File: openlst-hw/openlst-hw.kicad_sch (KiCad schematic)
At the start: 4 parts

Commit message: detailed power switches moved from EPS to invidual boards, each board only has core and aux bus (and batt if needed) which scales better. Reassign PC104 slots
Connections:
- no-connect marks 24 -> 20
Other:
- sheet CAN Bridge ports: added 3V3, 3V3_AUX, 3V3_COMM; removed VIO_CAN, VIO_CORE
- sheet INTERBOARD_CONNECTOR2 ports: added none; removed 3V3_17, 3V3_18, 3V3_19, 3V3_20

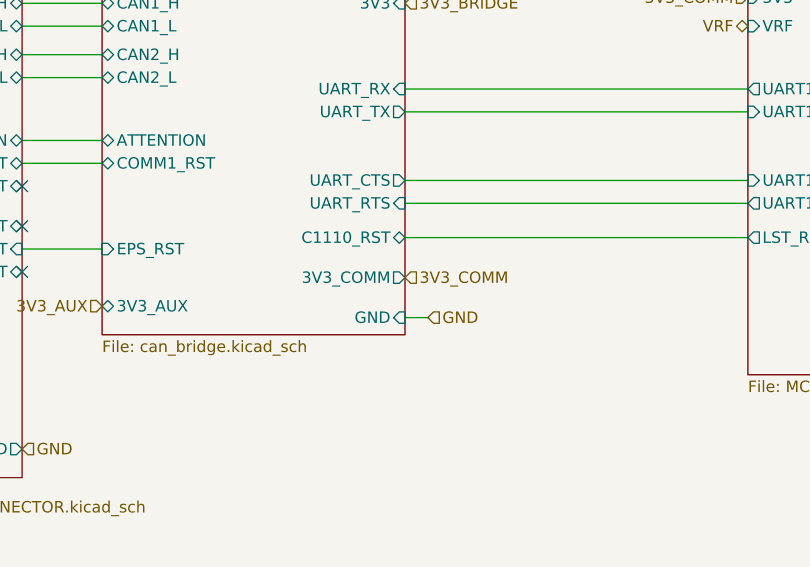
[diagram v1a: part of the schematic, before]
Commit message: rework COM board, add SPI ethernet for sat modem, upgrade all projects to 9.0.2
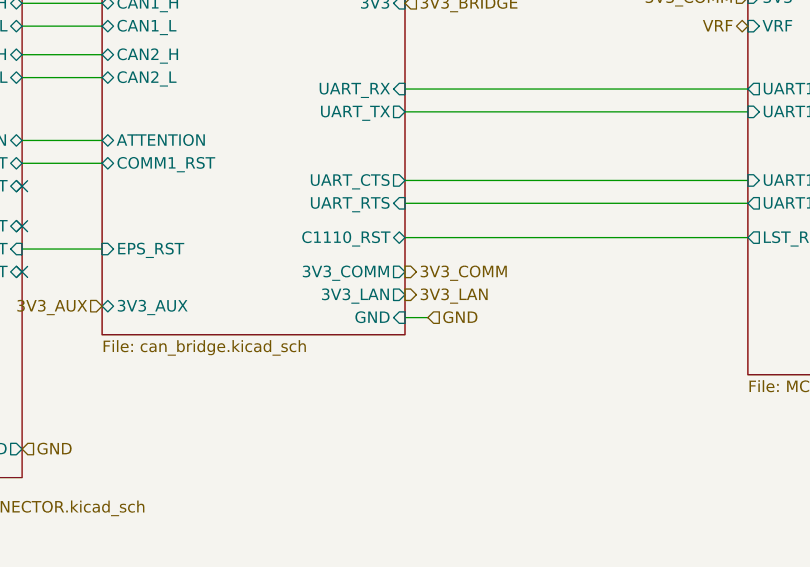
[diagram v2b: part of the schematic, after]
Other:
- sheet CAN Bridge ports: added 3V3_LAN; removed none
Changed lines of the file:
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@@
 (kicad_sch
-	(version 20231120)
+	(version 20250114)
 	(generator "eeschema")
-	(generator_version "8.0")
+	(generator_version "9.0")
 	(paper "A4")
 	(title_block
@@
 		(shape bidirectional)
 		(at 206.375 40.64 180)
-		(fields_autoplaced yes)
 		(effects
 			(font
@@
 		(shape output)
 		(at 109.855 108.585 180)
-		(fields_autoplaced yes)
 		(effects
 			(font
@@
 		(shape output)
 		(at 241.3 71.12 0)
-		(fields_autoplaced yes)
 		(effects
 			(font
@@
 		(shape bidirectional)
 		(at 154.305 40.005 180)
-		(fields_autoplaced yes)
 		(effects
 			(font
@@
 		)
 	)
+	(hierarchical_label "3V3_LAN"
+		(shape output)
+		(at 116.205 69.85 0)
+		(effects
+			(font
+				(size 1.27 1.27)
+			)
+			(justify left)
+		)
+	)
 	(hierarchical_label "GND"
 		(shape output)
 		(at 140.97 171.45 180)
-		(fields_autoplaced yes)
 		(effects
 			(font
@@
 		(shape input)
 		(at 45.72 52.705 180)
-		(fields_autoplaced yes)
 		(effects
 			(font
@@
 		(shape bidirectional)
 		(at 206.375 37.465 180)
-		(fields_autoplaced yes)
 		(effects
 			(font
@@
 		(shape output)
 		(at 191.135 76.835 0)
-		(fields_autoplaced yes)
 		(effects
 			(font
@@
 		(shape input)
 		(at 69.85 108.585 180)
-		(fields_autoplaced yes)
 		(effects
 			(font
@@
 		(shape input)
 		(at 118.745 72.39 0)
-		(fields_autoplaced yes)
 		(effects
 			(font
@@
 		(shape input)
 		(at 154.305 36.83 180)
-		(fields_autoplaced yes)
 		(effects
 			(font
@@
 		(shape input)
 		(at 98.425 108.585 180)
-		(fields_autoplaced yes)
 		(effects
 			(font
@@
 		(shape input)
 		(at 45.72 55.245 180)
-		(fields_autoplaced yes)
 		(effects
 			(font
@@
 		(shape input)
 		(at 116.205 37.465 0)
-		(fields_autoplaced yes)
 		(effects
 			(font
@@
 		(shape input)
 		(at 73.66 86.995 0)
-		(fields_autoplaced yes)
 		(effects
 			(font
@@
 		(shape input)
 		(at 86.36 108.585 180)
-		(fields_autoplaced yes)
 		(effects
 			(font
@@
 		(shape input)
 		(at 82.55 71.12 180)
-		(fields_autoplaced yes)
 		(effects
 			(font
@@
 		(shape input)
 		(at 45.72 29.21 180)
-		(fields_autoplaced yes)
 		(effects
 			(font
@@
 	)
 	(hierarchical_label "3V3_COMM"
-		(shape input)
-		(at 116.205 67.945 0)
-		(fields_autoplaced yes)
+		(shape output)
+		(at 116.205 67.31 0)
 		(effects
 			(font
@@
 		(at 45.72 24.13)
 		(size 27.94 66.04)
+		(exclude_from_sim no)
+		(in_bom yes)
+		(on_board yes)
+		(dnp no)
 		(stroke
 			(width 0)
@@
 		(at 82.55 34.925)
 		(size 33.655 39.37)
+		(exclude_from_sim no)
+		(in_bom yes)
+		(on_board yes)
+		(dnp no)
 		(fields_autoplaced yes)
 		(stroke
@@
 		)
 		(pin "3V3_COMM" output
-			(at 116.205 67.945 0)
+			(at 116.205 67.31 0)
 			(effects
 				(font
@@
 		(pin "3V3" input
 			(at 116.205 37.465 0)
+			(effects
+				(font
+					(size 1.27 1.27)
+				)
+				(justify right)
+			)
+		)
+		(pin "3V3_LAN" output
+			(at 116.205 69.85 0)
 			(effects
 				(font
@@
 		(at 206.375 35.56)
 		(size 30.48 39.37)
+		(exclude_from_sim no)
+		(in_bom yes)
+		(on_board yes)
+		(dnp no)
 		(fields_autoplaced yes)
 		(stroke
@@
 		(at 154.305 34.29)
 		(size 34.29 44.45)
+		(exclude_from_sim no)
+		(in_bom yes)
+		(on_board yes)
+		(dnp no)
 		(fields_autoplaced yes)
 		(stroke
@@
 		)
 	)
+	(embedded_fonts no)
 )

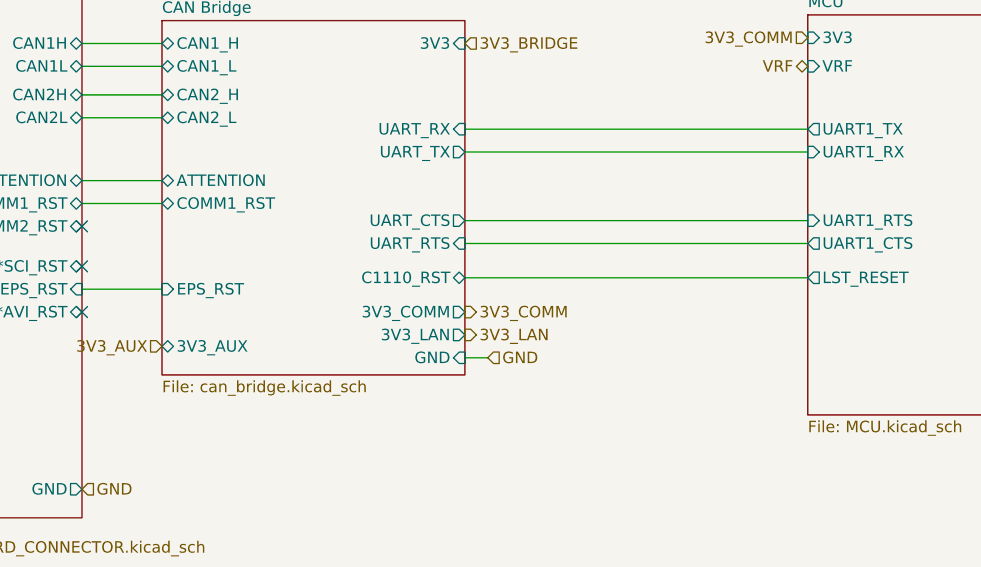
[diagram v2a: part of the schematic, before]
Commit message: sorting out pullups on resets and attention. replace reset with RN where possible. Introduce CN to save some parts
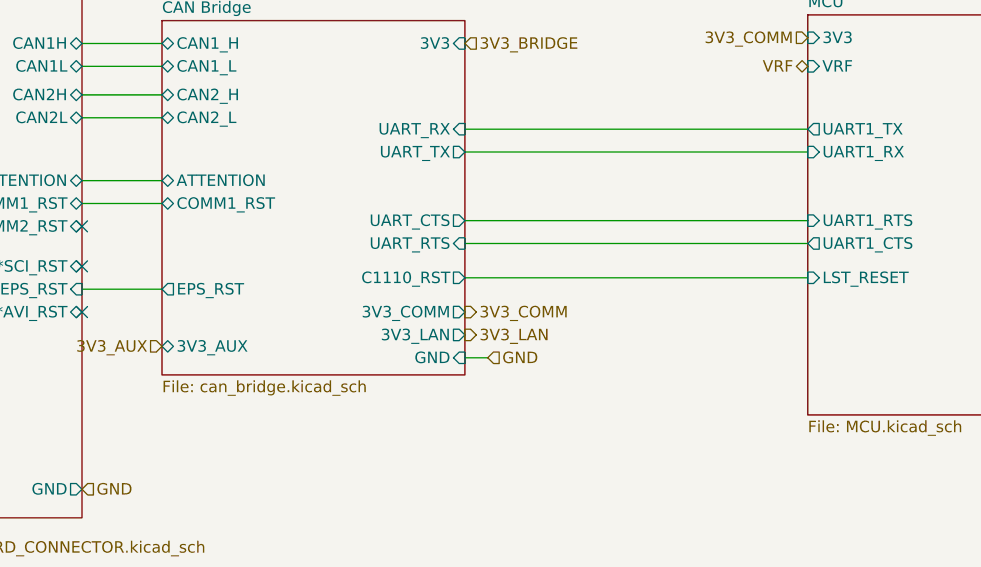
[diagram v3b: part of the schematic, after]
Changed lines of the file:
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@@
 			)
 		)
-		(pin "C1110_RST" bidirectional
+		(pin "C1110_RST" output
 			(at 116.205 63.5 0)
 			(effects
@@
 			)
 		)
-		(pin "EPS_RST" input
+		(pin "EPS_RST" output
 			(at 82.55 64.77 180)
 			(effects
@@
 			)
 		)
-		(pin "LST_RESET" output
+		(pin "LST_RESET" input
 			(at 154.305 63.5 180)
 			(effects
